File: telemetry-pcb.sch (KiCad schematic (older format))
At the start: 53 parts, among them CN1 12V_IN, CN10 CAN, CN11 CAN, CN12 CAN_12V_OUT, CN13 THERMO1, CN14 THERMO2, CN15 RS232, CN2 12V_OUT, CN3 12V_OUT, CN4 12V_OUT, CN5 12V_OUT, CN6 CAN, CN7 CAN, CN8 CAN, CN9 CAN, IC1 MAX31855K, IC2 MAX31855K, IC3 TCAN332DR, IC4 MAX3232CPWR, IC5 MCP2515-xSO, M1 MountingHole, M2 MountingHole, M3 MountingHole, M4 MountingHole, T1 TEST_12V, T2 TEST_3V3, T3 TEST_CAN, T4 GPIO_L, T5 GPIO_R, T6 TEST_RS232, Y1 8MHz

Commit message: revert before everything was messed up
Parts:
- added L1: RED, LED_SMD:LED_0805_2012Metric, symbol Device:LED
- added L2: GREEN, LED_SMD:LED_0805_2012Metric, symbol Device:LED
- added L3: BLUE, LED_SMD:LED_0805_2012Metric, symbol Device:LED
- added L4: YELLOW, LED_SMD:LED_0805_2012Metric, symbol Device:LED
- added R3, R5: 68, Resistor_SMD:R_0805_2012Metric, symbol Device:R
- added R4: 4.7, Resistor_SMD:R_0805_2012Metric, symbol Device:R
- added R6: 560, Resistor_SMD:R_0805_2012Metric, symbol Device:R
- added S2: AUX_BTN_1, TestPoint:TestPoint_2Pads_Pitch2.54mm_Drill0.8mm, symbol Connector:Conn_01x02_Female
- added S3: AUX_BTN_2, TestPoint:TestPoint_2Pads_Pitch2.54mm_Drill0.8mm, symbol Connector:Conn_01x02_Female
- added S4: AUX_BTN_3, TestPoint:TestPoint_2Pads_Pitch2.54mm_Drill0.8mm, symbol Connector:Conn_01x02_Female
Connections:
- wire segments 261 -> 290
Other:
- moved on the sheet: D1, T4, T5

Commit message: small changes and gerber file for JLPCB
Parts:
- L4: value YELLOW -> ORANGE
- R3: value 68 -> 5.6
- R4: value 4.7 -> 5.6
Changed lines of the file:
@@
 P 10400 5250
 F 0 "L4" V 10439 5132 50  0000 R CNN
-F 1 "YELLOW" V 10348 5132 50  0000 R CNN
+F 1 "ORANGE" V 10348 5132 50  0000 R CNN
 F 2 "LED_SMD:LED_0805_2012Metric" H 10400 5250 50  0001 C CNN
 F 3 "~" H 10400 5250 50  0001 C CNN
@@
 P 11300 4750
 F 0 "R3" H 11370 4796 50  0000 L CNN
-F 1 "68" H 11370 4705 50  0000 L CNN
+F 1 "5.6" H 11370 4705 50  0000 L CNN
 F 2 "Resistor_SMD:R_0805_2012Metric" V 11230 4750 50  0001 C CNN
 F 3 "~" H 11300 4750 50  0001 C CNN
@@
 P 10850 4750
 F 0 "R4" H 10920 4796 50  0000 L CNN
-F 1 "4.7" H 10920 4705 50  0000 L CNN
+F 1 "5.6" H 10920 4705 50  0000 L CNN
 F 2 "Resistor_SMD:R_0805_2012Metric" V 10780 4750 50  0001 C CNN
 F 3 "~" H 10850 4750 50  0001 C CNN

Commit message: started on 1.1 redesign, schematic is done and PCB has just been started.
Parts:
- removed C1, C15, C2, C3, C4, C5, C6, C7, C8: 0.1uF, Capacitor_SMD:C_0805_2012Metric, symbol Device:C
- removed C10, C9: 0.01uF, Capacitor_SMD:C_0805_2012Metric, symbol Device:C
- removed C11, C12: 22pF, Capacitor_SMD:C_0805_2012Metric, symbol Device:C
- removed C13: 10uF, Capacitor_SMD:C_1206_3216Metric, symbol Device:CP
- removed C14: 47uF, Capacitor_SMD:CP_Elec_6.3x5.4, symbol Device:CP
- removed CN1: 12V_IN, Connector_Molex:Molex_Mega-Fit_76825-0004_2x02_P5.70mm_Horizontal, symbol Connector_Generic:Conn_01x04
- removed CN10, CN11, CN6, CN7, CN8, CN9: CAN, Conn_Molex_70553-0001:Molex-70553-0001-0-0-MFG, symbol Connector_Generic:Conn_01x02
- removed CN12: CAN_12V_OUT, Connector_Molex:Molex_Mega-Fit_76825-0010_2x05_P5.70mm_Horizontal, symbol Connector_Generic:Conn_02x05_Counter_Clockwise
- removed CN13: THERMO1, Conn_Molex_70553-0002:Molex-70551-0002-0-0-0, symbol Connector_Generic:Conn_01x03
- removed CN14: THERMO2, Conn_Molex_70553-0002:Molex-70551-0002-0-0-0, symbol Connector_Generic:Conn_01x03
- removed CN15: RS232, Libraries:DLS1XP5AK40X, symbol Connector:DB9_Male
- removed CN2, CN3, CN4, CN5: 12V_OUT, Connector_Molex:Molex_Mega-Fit_76825-0004_1x02_P5.70mm_Horizontal, symbol Connector_Generic:Conn_01x02
- removed D1: 1A 50v, Diode_SMD:D_SMA, symbol Device:D
- removed F1: 25A, Fuse:Fuseholder_Blade_Mini_Keystone_3568, symbol Device:Fuse
- removed IC1, IC2: MAX31855K, Package_SO:SOIC-8-1EP_3.9x4.9mm_P1.27mm_EP2.29x3mm, symbol telemetry-pcb-eagle-import:MAX31855K
- removed IC3: TCAN332DR, Libraries:SOIC127P599X175-8N, symbol TCAN332DR:TCAN332DR
- removed IC4: MAX3232CPWR, Package_SO:TSSOP-16_4.4x5mm_P0.65mm, symbol MAX3232CPWR:MAX3232CPWR
- removed IC5: MCP2515-xSO, Package_SO:SOIC-18W_7.5x11.6mm_P1.27mm, symbol Interface_CAN_LIN:MCP2515-xSO
- removed L1: RED, LED_SMD:LED_0805_2012Metric, symbol Device:LED
- removed M1, M2, M3, M4: MountingHole, MountingHole:MountingHole_3.2mm_M3, symbol Mechanical:MountingHole
- removed R1: 120, Resistor_SMD:R_0805_2012Metric, symbol Device:R
- removed R2: 10K, Resistor_SMD:R_0805_2012Metric, symbol Device:R
- removed R6: 560, Resistor_SMD:R_0805_2012Metric, symbol Device:R
- removed S1: CAN_TERM, Button_Switch_THT:SW_DIP_SPSTx01_Piano_10.8x4.1mm_W7.62mm_P2.54mm, symbol Switch:SW_DIP_x01
- removed S2: AUX_BTN_1, TestPoint:TestPoint_2Pads_Pitch2.54mm_Drill0.8mm, symbol Connector:Conn_01x02_Female
- removed S4: AUX_BTN_3, TestPoint:TestPoint_2Pads_Pitch2.54mm_Drill0.8mm, symbol Connector:Conn_01x02_Female
- removed T2: TEST_3V3, TestPoint:TestPoint_2Pads_Pitch2.54mm_Drill0.8mm, symbol Connector:Conn_01x02_Female
- removed T3: TEST_CAN, TestPoint:TestPoint_2Pads_Pitch2.54mm_Drill0.8mm, symbol Connector:Conn_01x02_Female
- removed T6: TEST_RS232, TestPoint:TestPoint_2Pads_Pitch2.54mm_Drill0.8mm, symbol Connector:Conn_01x02_Female
- removed Y1: 8MHz, Crystal:Crystal_SMD_HC49-SD, symbol Device:Crystal
- H1,H2: footprint Libraries:PCB_FeatherWing -> telemetry-pcb:Particle_boron; symbol particle:Particle_Boron -> telemetry-pcb-rescue:Particle_Boron-particle-telemetry-pcb-rescue
- S3: value AUX_BTN_2 -> LOG_BTN
- T1: value TEST_12V -> TEST_3V3
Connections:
- net labels removed: +12V, CANH, CANL
- wire segments 290 -> 103
- no-connect marks 23 -> 4
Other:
- moved on the sheet: L2, L3, L4, R3, R4, R5, S3, T4, T5

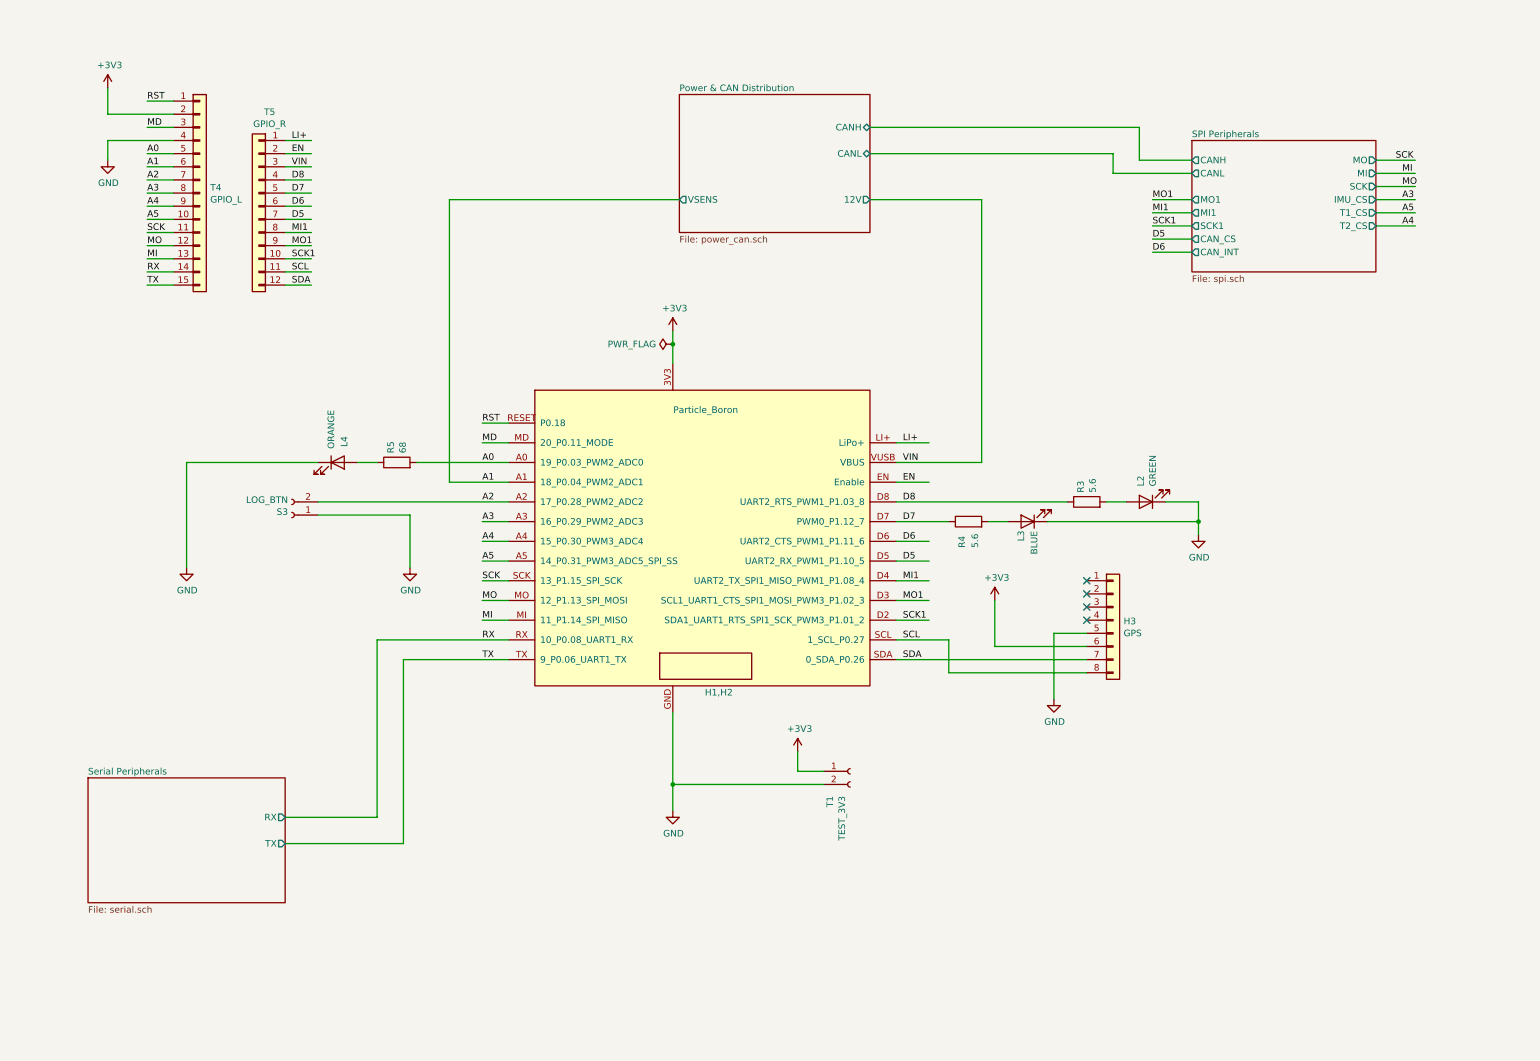
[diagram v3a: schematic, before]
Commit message: finished schematic and PCB layout for 1.1 board
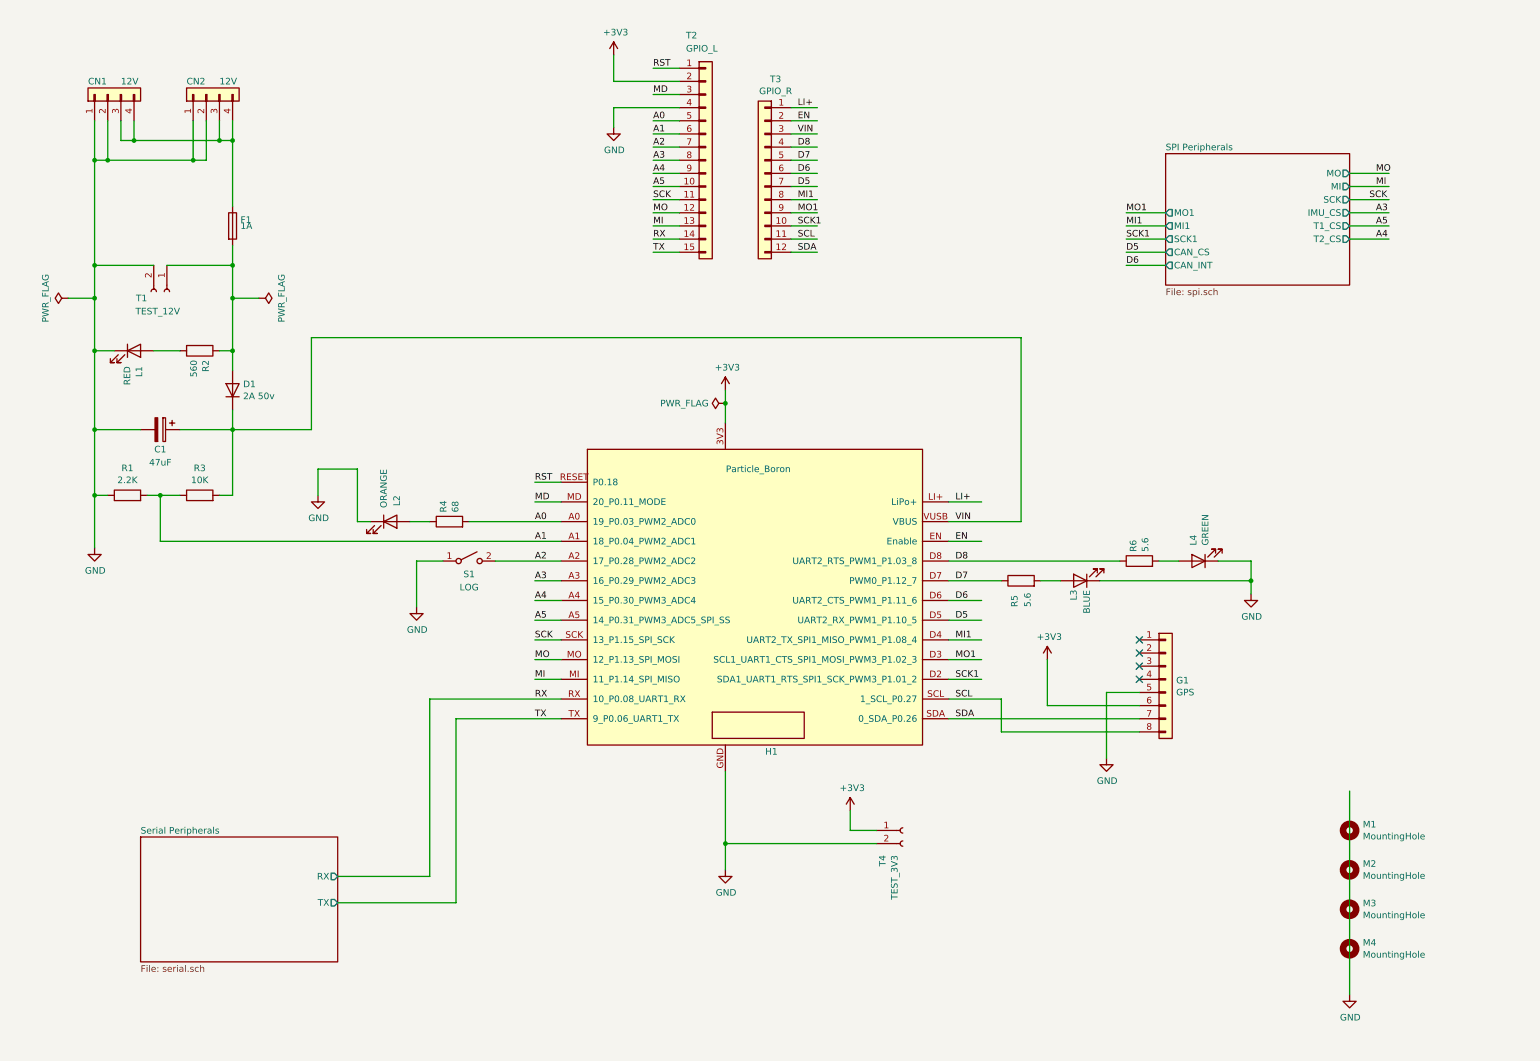
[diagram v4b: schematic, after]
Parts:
- removed S3: LOG_BTN, TestPoint:TestPoint_2Pads_Pitch2.54mm_Drill0.8mm, symbol Connector:Conn_01x02_Female
- added C1: 47uF, Capacitor_SMD:CP_Elec_6.3x5.4, symbol Device:CP
- added CN1, CN2: 12V, telemetry-pcb:molex_sl_1x04_horizontal, symbol Connector_Generic:Conn_01x04
- added D1: 2A 50v, Diode_SMD:D_SMA, symbol Device:D
- added F1: 1A, telemetry-pcb:0154001.DRL, symbol Device:Fuse
- added L1: RED, LED_SMD:LED_0805_2012Metric, symbol Device:LED
- added M1, M2, M3, M4: MountingHole, MountingHole:MountingHole_3.2mm_M3, symbol Mechanical:MountingHole
- added R1: 2.2K, Resistor_SMD:R_0805_2012Metric, symbol Device:R
- added R2: 560, Resistor_SMD:R_0805_2012Metric, symbol Device:R
- added R3: 10K, Resistor_SMD:R_0805_2012Metric, symbol Device:R
- added S1: LOG, Button_Switch_THT:SW_PUSH_6mm_H13mm, symbol Switch:SW_SPST
- added T1: TEST_12V, TestPoint:TestPoint_2Pads_Pitch2.54mm_Drill0.8mm, symbol Connector:Conn_01x02_Female
- G1: renamed from H3; footprint Connector_PinSocket_2.54mm:PinSocket_1x08_P2.54mm_Vertical -> telemetry-pcb:Sparkfun GPS
- renumbered H1,H2 to H1, L4 to L2, L2 to L4, R5 to R4, R4 to R5, R3 to R6, T4 to T2, T5 to T3, T1 to T4
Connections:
- wire segments 103 -> 141
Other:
- moved on the sheet: G1, H1, L2, L3, L4, R4, R5, R6, T2, T3, T4

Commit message: routed all
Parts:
- T2: footprint Connector_PinSocket_2.54mm:PinSocket_1x15_P2.54mm_Vertical -> telemetry-pcb:Boron_Pins_L
- T3: footprint Connector_PinSocket_2.54mm:PinSocket_1x12_P2.54mm_Vertical -> telemetry-pcb:Boron_Pins_R
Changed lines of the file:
@@
 F 0 "T2" H 5350 2250 50  0000 L CNN
 F 1 "GPIO_L" H 5350 2150 50  0000 L CNN
-F 2 "Connector_PinSocket_2.54mm:PinSocket_1x15_P2.54mm_Vertical" H 5500 1300 50  0001 C CNN
+F 2 "telemetry-pcb:Boron_Pins_L" H 5500 1300 50  0001 C CNN
 F 3 "~" H 5500 1300 50  0001 C CNN
 	1    5500 1300
@@
 F 0 "T3" H 5868 2117 50  0000 C CNN
 F 1 "GPIO_R" H 5868 2026 50  0000 C CNN
-F 2 "Connector_PinSocket_2.54mm:PinSocket_1x12_P2.54mm_Vertical" H 5950 1400 50  0001 C CNN
+F 2 "telemetry-pcb:Boron_Pins_R" H 5950 1400 50  0001 C CNN
 F 3 "~" H 5950 1400 50  0001 C CNN
 	1    5950 1400

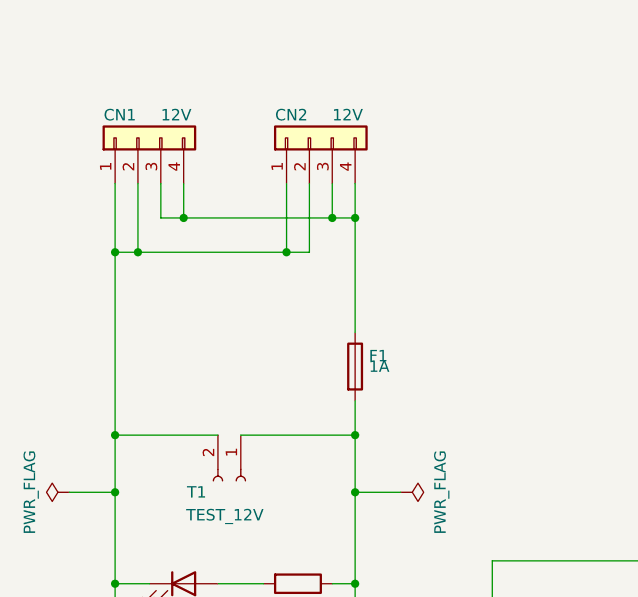
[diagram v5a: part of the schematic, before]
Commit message: removes one power port, changes CAN switch to jumper
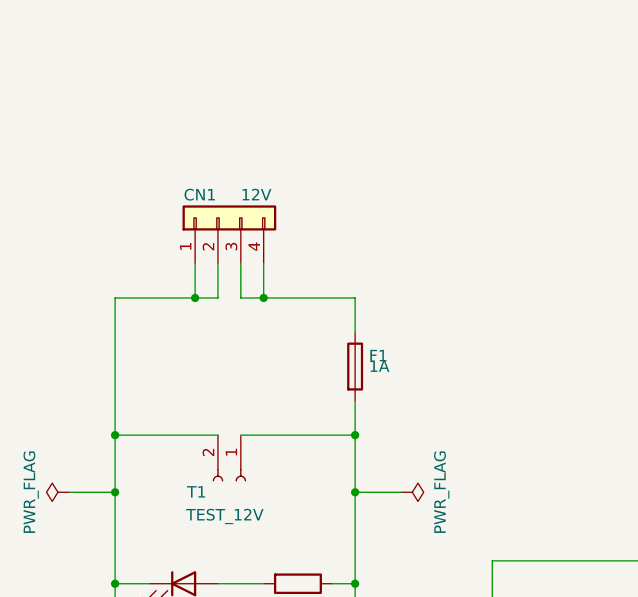
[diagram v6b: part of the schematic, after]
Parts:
- removed CN2: 12V, telemetry-pcb:molex_sl_1x04_horizontal, symbol Connector_Generic:Conn_01x04
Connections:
- wire segments 141 -> 135
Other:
- moved on the sheet: CN1
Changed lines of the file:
@@
 L Connector_Generic:Conn_01x04 CN1
 U 1 1 621A168A
-P 950 800
+P 1300 1150
 AR Path="/621A168A" Ref="CN1"  Part="1"
 AR Path="/6188C66E/621A168A" Ref="CN?"  Part="1"
-F 0 "CN1" V 1050 950 50  0000 R CNN
-F 1 "12V" V 1050 700 50  0000 R CNN
-F 2 "telemetry-pcb:molex_sl_1x04_horizontal" H 950 800 50  0001 C CNN
-F 3 "~" H 950 800 50  0001 C CNN
-	1    950  800
+F 0 "CN1" V 1400 1300 50  0000 R CNN
+F 1 "12V" V 1400 1050 50  0000 R CNN
+F 2 "telemetry-pcb:molex_sl_1x04_horizontal" H 1300 1150 50  0001 C CNN
+F 3 "~" H 1300 1150 50  0001 C CNN
+	1    1300 1150
 	0    -1   -1   0
 $EndComp
@@
 Wire Wire Line
 	3300 4350 3300 4700
-$Comp
-L Connector_Generic:Conn_01x04 CN2
-U 1 1 625FC8D1
-P 1700 800
-AR Path="/625FC8D1" Ref="CN2"  Part="1"
-AR Path="/6188C66E/625FC8D1" Ref="CN?"  Part="1"
-F 0 "CN2" V 1800 950 50  0000 R CNN
-F 1 "12V" V 1800 700 50  0000 R CNN
-F 2 "telemetry-pcb:molex_sl_1x04_horizontal" H 1700 800 50  0001 C CNN
-F 3 "~" H 1700 800 50  0001 C CNN
-	1    1700 800
-	0    -1   -1   0
-$EndComp
 Connection ~ 850  2350
 Wire Wire Line
@@
 Connection ~ 1900 2100
 Wire Wire Line
-	1800 1000 1800 1150
-Wire Wire Line
-	1800 1150 1900 1150
-Wire Wire Line
-	1900 1150 1900 1000
-Wire Wire Line
-	1150 1150 1150 1000
-Connection ~ 1800 1150
-Wire Wire Line
-	1050 1150 1050 1000
-Wire Wire Line
-	1150 1150 1800 1150
-Wire Wire Line
-	1050 1150 1150 1150
-Connection ~ 1150 1150
-Wire Wire Line
-	850  1000 850  1300
+	1900 1950 1900 2100
+Wire Wire Line
+	850  2100 850  2350
+Wire Wire Line
+	7900 2650 7900 4050
+Wire Wire Line
+	2500 2650 7900 2650
+Wire Wire Line
+	7900 4050 7350 4050
+Wire Wire Line
+	1900 1650 1900 1500
+Wire Wire Line
+	1900 1500 1500 1500
+Wire Wire Line
+	1500 1500 1500 1350
+Wire Wire Line
+	1400 1350 1400 1500
+Wire Wire Line
+	1400 1500 1500 1500
+Connection ~ 1500 1500
+Wire Wire Line
+	1300 1350 1300 1500
+Wire Wire Line
+	1300 1500 1200 1500
+Wire Wire Line
+	850  1500 850  2100
 Connection ~ 850  2100
 Wire Wire Line
-	950  1000 950  1300
-Wire Wire Line
-	950  1300 850  1300
-Connection ~ 850  1300
-Wire Wire Line
-	850  1300 850  2100
-Wire Wire Line
-	950  1300 1600 1300
-Wire Wire Line
-	1600 1300 1600 1000
-Connection ~ 950  1300
-Wire Wire Line
-	1700 1000 1700 1300
-Wire Wire Line
-	1700 1300 1600 1300
-Connection ~ 1600 1300
-Wire Wire Line
-	1900 1950 1900 2100
-Wire Wire Line
-	850  2100 850  2350
-Wire Wire Line
-	1900 1150 1900 1650
-Connection ~ 1900 1150
-Wire Wire Line
-	7900 2650 7900 4050
-Wire Wire Line
-	2500 2650 7900 2650
-Wire Wire Line
-	7900 4050 7350 4050
+	1200 1350 1200 1500
+Connection ~ 1200 1500
+Wire Wire Line
+	1200 1500 850  1500
 $EndSCHEMATC

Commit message: Updates BOM
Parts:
- R2: value 560 -> 680
- R5: value 5.6 -> 6.8
- R6: value 5.6 -> 150
- renumbered G1 to H2
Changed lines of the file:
@@
 AR Path="/6188C66E/621A16B6" Ref="R?"  Part="1"
 F 0 "R2" H 1720 2796 50  0000 L CNN
-F 1 "560" H 1720 2705 50  0000 L CNN
+F 1 "680" H 1720 2705 50  0000 L CNN
 F 2 "Resistor_SMD:R_0805_2012Metric" V 1580 2750 50  0001 C CNN
 F 3 "~" H 1650 2750 50  0001 C CNN
@@
 P 7900 4500
 F 0 "R5" H 7700 4550 50  0000 L CNN
-F 1 "5.6" H 7700 4450 50  0000 L CNN
+F 1 "6.8" H 7700 4450 50  0000 L CNN
 F 2 "Resistor_SMD:R_0805_2012Metric" V 7830 4500 50  0001 C CNN
 F 3 "~" H 7900 4500 50  0001 C CNN
@@
 P 8800 4350
 F 0 "R6" H 8870 4396 50  0000 L CNN
-F 1 "5.6" H 8870 4305 50  0000 L CNN
+F 1 "150" H 8870 4305 50  0000 L CNN
 F 2 "Resistor_SMD:R_0805_2012Metric" V 8730 4350 50  0001 C CNN
 F 3 "~" H 8800 4350 50  0001 C CNN
@@
 $EndSheet
 $Comp
-L Connector_Generic:Conn_01x08 G1
+L Connector_Generic:Conn_01x08 H2
 U 1 1 61991C85
 P 9000 5250
-AR Path="/61991C85" Ref="G1"  Part="1"
+AR Path="/61991C85" Ref="H2"  Part="1"
 AR Path="/61951597/61991C85" Ref="G?"  Part="1"
-F 0 "G1" H 9080 5242 50  0000 L CNN
+F 0 "H2" H 9080 5242 50  0000 L CNN
 F 1 "GPS" H 9080 5151 50  0000 L CNN
 F 2 "telemetry-pcb:Sparkfun GPS" H 9000 5250 50  0001 C CNN

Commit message: deleted extraneous footprints
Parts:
- H1: symbol telemetry-pcb-rescue:Particle_Boron-particle-telemetry-pcb-rescue -> telemetry-pcb-rescue:Particle_Boron-particle-telemetry-pcb-rescue-telemetry-pcb-rescue
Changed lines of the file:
@@
 $EndComp
 $Comp
-L telemetry-pcb-rescue:Particle_Boron-particle-telemetry-pcb-rescue H1
+L telemetry-pcb-rescue:Particle_Boron-particle-telemetry-pcb-rescue-telemetry-pcb-rescue H1
 U 1 1 602A0E66
 P 5850 4500
